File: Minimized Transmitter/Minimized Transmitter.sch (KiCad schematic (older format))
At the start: 1 part

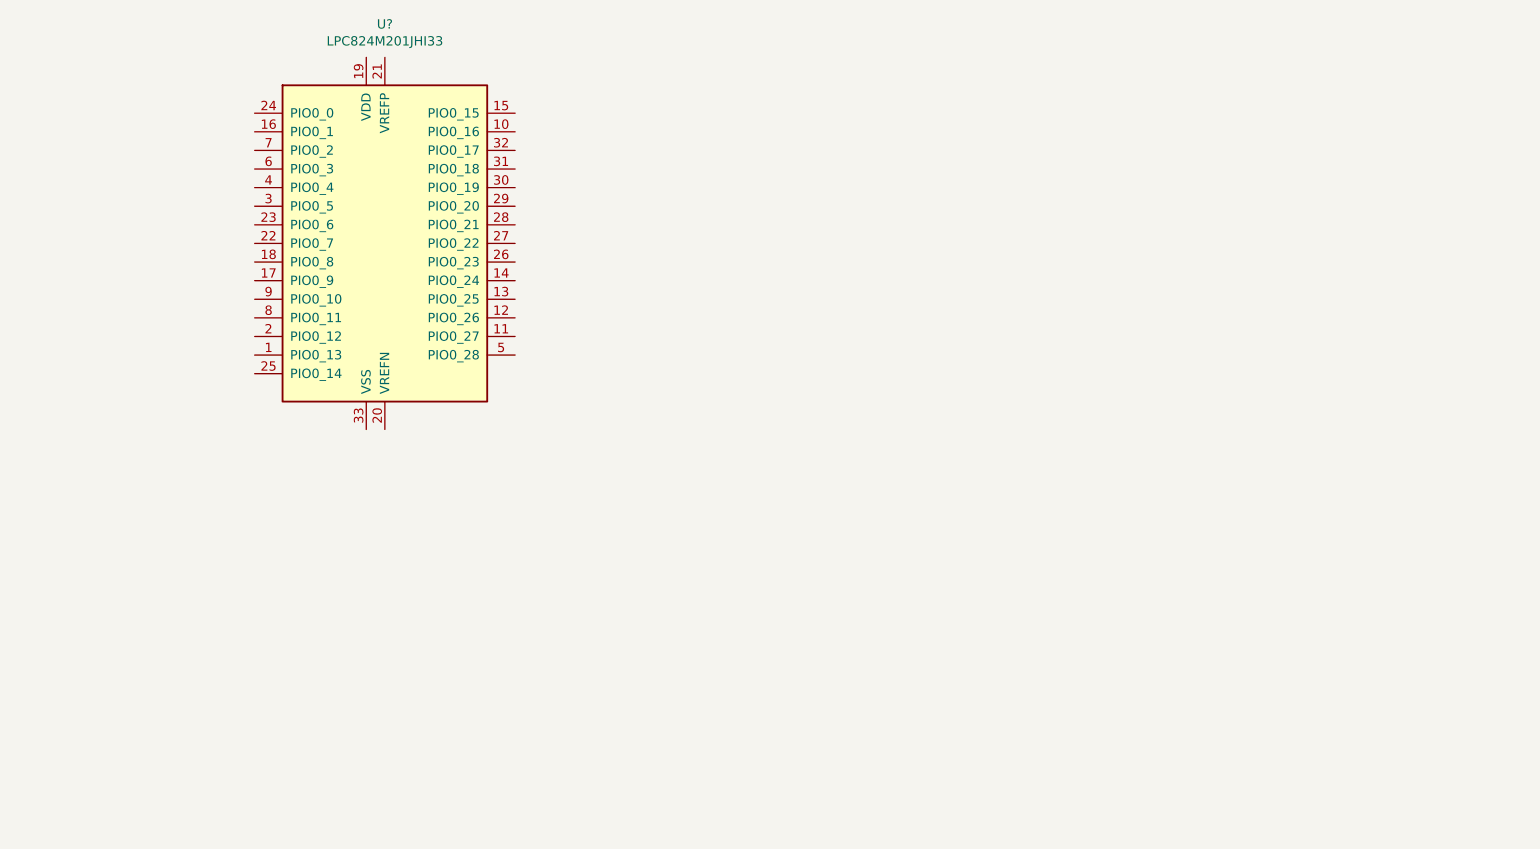
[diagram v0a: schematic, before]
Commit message: inished Minimized Disc Transmitter
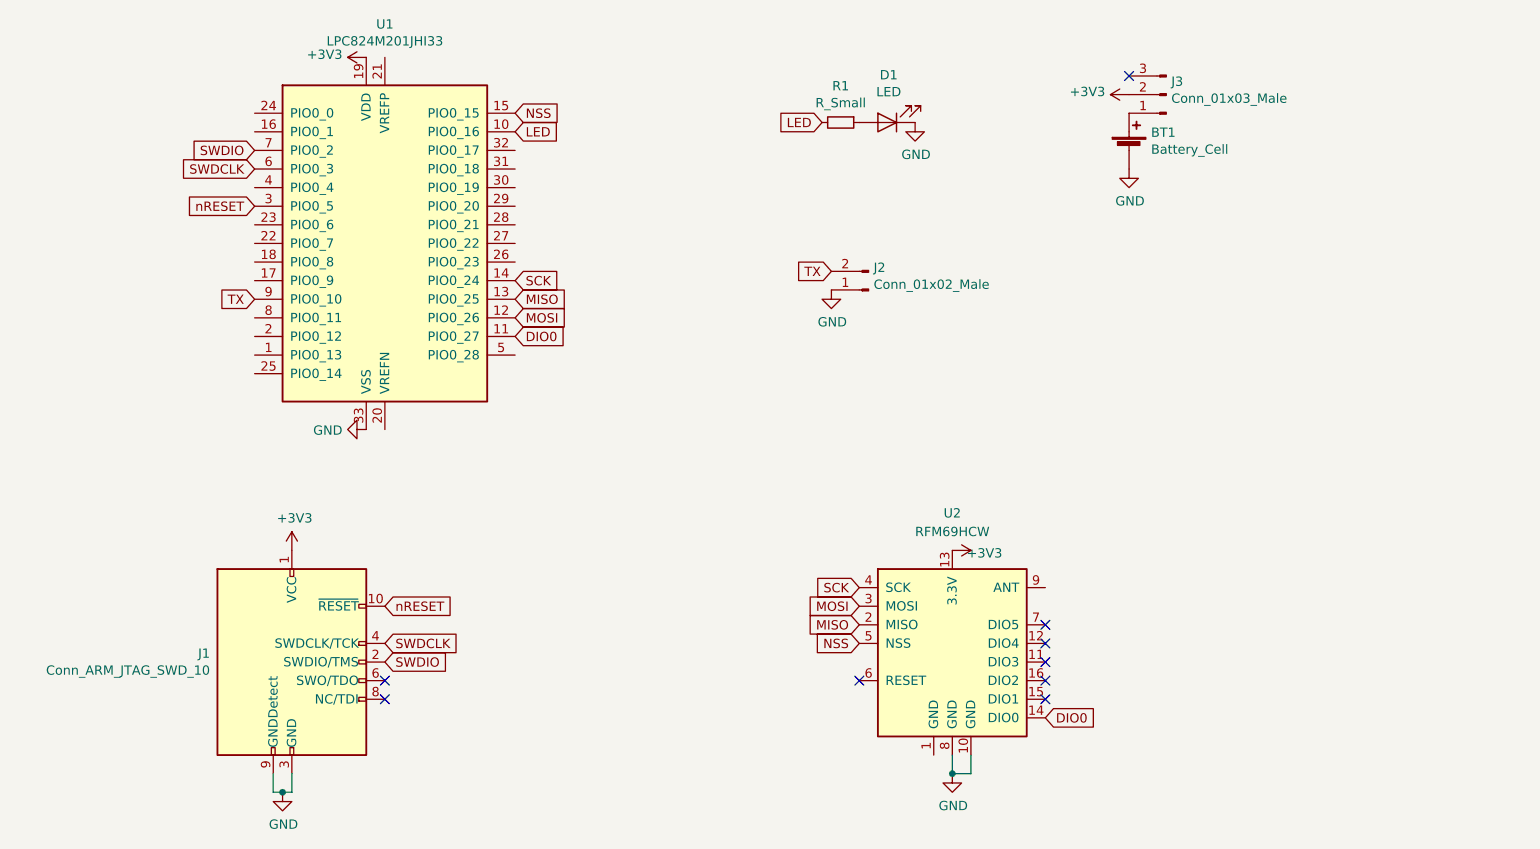
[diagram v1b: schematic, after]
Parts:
- added BT1: Battery_Cell, my_foot_prints:PRT-11892, symbol Device:Battery_Cell
- added D1: LED, LED_SMD:LED_1206_3216Metric, symbol Device:LED
- added J1: Conn_ARM_JTAG_SWD_10, Connector_PinHeader_1.27mm:PinHeader_2x05_P1.27mm_Vertical_SMD, symbol Connector:Conn_ARM_JTAG_SWD_10
- added J2: Conn_01x02_Male, Connector_PinHeader_2.54mm:PinHeader_1x02_P2.54mm_Vertical, symbol Connector:Conn_01x02_Male
- added J3: Conn_01x03_Male, Connector_PinHeader_2.54mm:PinHeader_1x03_P2.54mm_Vertical, symbol Connector:Conn_01x03_Male
- added R1: R_Small, Resistor_SMD:R_0402_1005Metric, symbol Device:R_Small
- added U2: RFM69HCW, my_foot_prints:RFM96HCW, symbol RF_AM_FM:RFM69HCW
- gave numbers to parts that had none: 1
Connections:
- net LED: now reaches U1.10 (PIO0_16)
- net LED: now also R1.2
- net DIO0: now reaches U1.11 (PIO0_27)
- net DIO0: now also U2.14 (DIO0)
- net MOSI: now reaches U1.12 (PIO0_26)
- net MOSI: now also U2.3 (MOSI)
- net MISO: now reaches U1.13 (PIO0_25)
- net MISO: now also U2.2 (MISO)
- net SCK: now reaches U1.14 (PIO0_24)
- net SCK: now also U2.4 (SCK)
- net NSS: now reaches U1.15 (PIO0_15)
- net NSS: now also U2.5 (NSS)
- net +3V3: now reaches U1.19 (VDD)
- net +3V3: now also J1.1 (VCC), J3.2 (Pin_2), U2.13 (3.3V)
- net nRESET: now reaches U1.3 (PIO0_5)
- net nRESET: now also J1.10 (~RESET~)
- net GND: now reaches U1.33 (VSS)
- net GND: now also BT1.2 (-), D1.1 (K), J1.3 (GND), J1.5 (GND), J1.9 (GNDDetect), J2.1 (Pin_1), U2.10 (GND), U2.8 (GND)
- net SWDCLK: now reaches U1.6 (PIO0_3)
- net SWDCLK: now also J1.4 (SWDCLK/TCK)
- net SWDIO: now reaches U1.7 (PIO0_2)
- net SWDIO: now also J1.2 (SWDIO/TMS)
- net TX: now reaches U1.9 (PIO0_10)
- net TX: now also J2.2 (Pin_2)
- new net: D1.2 (A), R1.1
- new net: BT1.1 (+), J3.1 (Pin_1)
- no-connect marks 0 -> 9

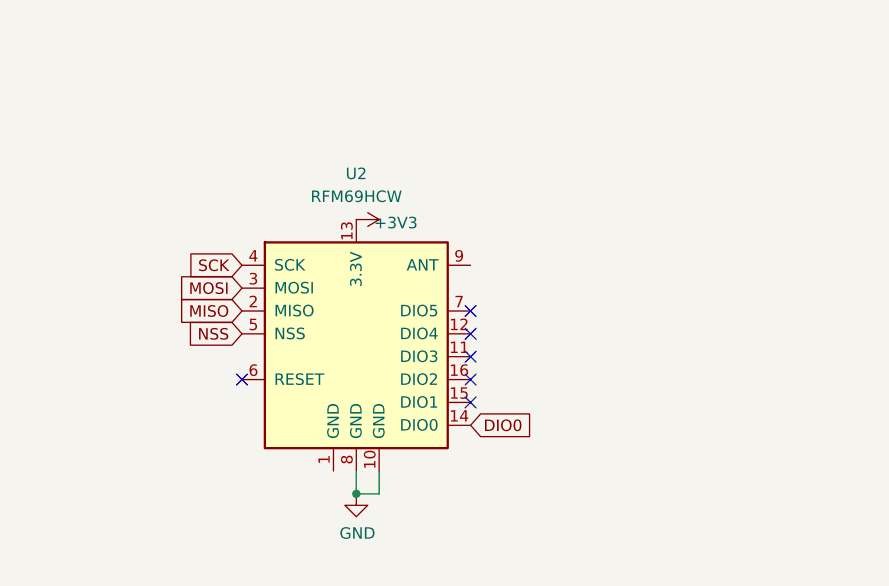
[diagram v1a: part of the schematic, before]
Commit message: Fixed pads on RFM footprint
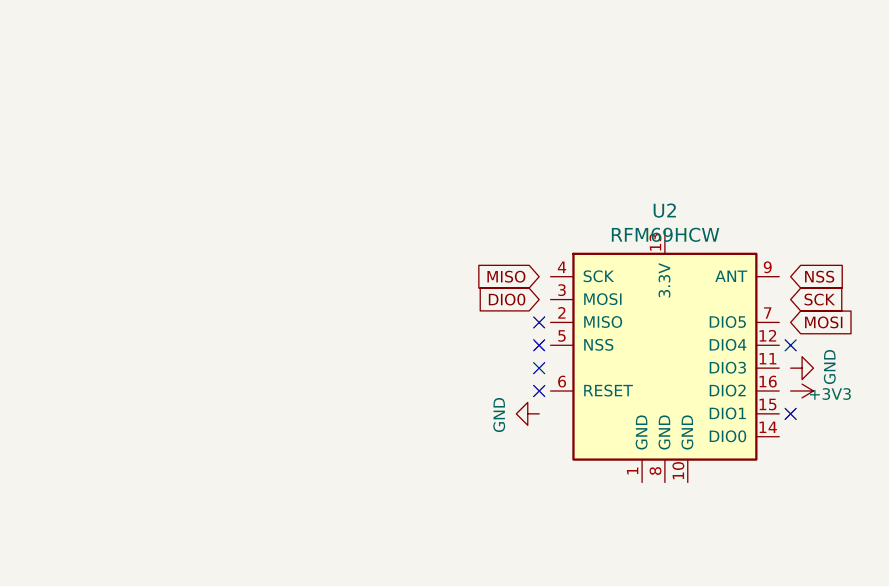
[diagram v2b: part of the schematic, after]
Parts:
- removed U2: RFM69HCW, my_foot_prints:RFM96HCW, symbol RF_AM_FM:RFM69HCW
- added U2: RFM69HCW, my_foot_prints:RFM96HCW, symbol Transmitter~board-rescue:RFM69HCW
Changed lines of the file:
@@
-$EndComp
-$Comp
-L RF_AM_FM:RFM69HCW U2
-U 1 1 5BDB3040
-P 5550 4450
-F 0 "U2" H 5550 5150 50  0000 C CNN
-F 1 "RFM69HCW" H 5550 5050 50  0000 C CNN
-F 2 "my_foot_prints:RFM96HCW" H 2250 6100 50  0001 C CNN
-F 3 "http://www.hoperf.com/upload/rf/RFM69HCW-V1.1.pdf" H 2250 6100 50  0001 C CNN
-	1    5550 4450
-	1    0    0    -1
 $EndComp
 $Comp
@@
 	0    1    1    0
 $EndComp
-Text GLabel 5050 4250 0    50   Input ~ 0
+Text GLabel 7450 4400 2    50   Input ~ 0
 MOSI
-Text GLabel 5050 4350 0    50   Input ~ 0
+Text GLabel 6350 4200 0    50   Input ~ 0
 MISO
-Text GLabel 5050 4450 0    50   Input ~ 0
+Text GLabel 7450 4200 2    50   Input ~ 0
 NSS
-Text GLabel 5050 4150 0    50   Input ~ 0
+Text GLabel 7450 4300 2    50   Input ~ 0
 SCK
 Text GLabel 3200 2800 2    50   Input ~ 0
@@
 L power:GND #PWR0101
 U 1 1 5BDB3517
-P 5550 5150
-F 0 "#PWR0101" H 5550 4900 50  0001 C CNN
-F 1 "GND" H 5555 4977 50  0000 C CNN
-F 2 "" H 5550 5150 50  0001 C CNN
-F 3 "" H 5550 5150 50  0001 C CNN
-	1    5550 5150
-	1    0    0    -1
-$EndComp
-Wire Wire Line
-	5550 5050 5550 5150
-Connection ~ 5550 5150
-Wire Wire Line
-	5650 5050 5650 5150
-Wire Wire Line
-	5650 5150 5550 5150
+P 7450 4600
+F 0 "#PWR0101" H 7450 4350 50  0001 C CNN
+F 1 "GND" H 7455 4427 50  0000 C CNN
+F 2 "" H 7450 4600 50  0001 C CNN
+F 3 "" H 7450 4600 50  0001 C CNN
+	1    7450 4600
+	0    -1   -1   0
+$EndComp
 $Comp
 L power:+3V3 #PWR0102
 U 1 1 5BDB3592
-P 5550 3950
-F 0 "#PWR0102" H 5550 3800 50  0001 C CNN
-F 1 "+3V3" V 5565 4123 50  0000 C CNN
-F 2 "" H 5550 3950 50  0001 C CNN
-F 3 "" H 5550 3950 50  0001 C CNN
-	1    5550 3950
+P 7450 4700
+F 0 "#PWR0102" H 7450 4550 50  0001 C CNN
+F 1 "+3V3" V 7465 4873 50  0000 C CNN
+F 2 "" H 7450 4700 50  0001 C CNN
+F 3 "" H 7450 4700 50  0001 C CNN
+	1    7450 4700
 	0    1    1    0
 $EndComp
@@
 Text GLabel 3200 2500 2    50   Input ~ 0
 SCK
-Text GLabel 6050 4850 2    50   Input ~ 0
+Text GLabel 6350 4300 0    50   Input ~ 0
 DIO0
 $Comp
@@
 $EndComp
 NoConn ~ 6500 1400
-NoConn ~ 6050 4750
-NoConn ~ 6050 4650
-NoConn ~ 6050 4550
-NoConn ~ 6050 4450
-NoConn ~ 6050 4350
-NoConn ~ 5050 4650
+NoConn ~ 7450 4500
+NoConn ~ 6350 4700
+NoConn ~ 6350 4600
+NoConn ~ 6350 4500
+NoConn ~ 6350 4400
+NoConn ~ 7450 4800
 Text GLabel 4900 2450 0    50   Input ~ 0
 TX
@@
 	1    0    0    -1
 $EndComp
+$Comp
+L Transmitter~board-rescue:RFM69HCW U2
+U 1 1 5C15B19A
+P 6900 4500
+F 0 "U2" H 6900 5087 60  0000 C CNN
+F 1 "RFM69HCW" H 6900 4981 60  0000 C CNN
+F 2 "my_foot_prints:RFM96HCW" H 6900 4550 60  0001 C CNN
+F 3 "" H 6900 4550 60  0001 C CNN
+	1    6900 4500
+	1    0    0    -1
+$EndComp
+$Comp
+L power:GND #PWR0111
+U 1 1 5C15B399
+P 6350 4800
+F 0 "#PWR0111" H 6350 4550 50  0001 C CNN
+F 1 "GND" H 6355 4627 50  0000 C CNN
+F 2 "" H 6350 4800 50  0001 C CNN
+F 3 "" H 6350 4800 50  0001 C CNN
+	1    6350 4800
+	0    1    1    0
+$EndComp
 $EndSCHEMATC
